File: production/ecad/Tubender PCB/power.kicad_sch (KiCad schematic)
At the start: 68 parts, among them J30 640387-2, U1 LMR36520FADDAR, U12 LM5146RGYR, U13 LM5017SDX/NOPB, U5 TPSM265R1V5SILR

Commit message: start power layout
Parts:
- CBOOT33, C_BST2, C_BST3, C_C1, C_C2, C_C3, C_HF33, C_ILIM1, C_IN2, C_IN33, C_IN5, C_OUT12, C_OUT2, C_OUT3, C_OUT33, C_SS1, C_VCC2, C_VCC3, C_VCC33, C_VIN1, C_VIN2: footprint (none) -> Capacitor_SMD:C_0805_2012Metric
- D10, D6, D7, D8, D9: footprint WL-SMCW_0603:WL-SMCW_0603 -> ${KIPRJMOD}:WL-SMCW_0603
- J30: footprint 640387-2:TE_640387-2 -> ${KIPRJMOD}:TE_640387-2
- L1, L2, L_SW2: footprint (none) -> Inductor_SMD:L_0805_2012Metric
- R1, R2, R20, R22, R3, R46, R47, R_C1, R_C2, R_FB1, R_FB2, R_ILIM1, R_IND12, R_IND24, R_IND3, R_IND48, R_IND5, R_ON1, R_OUT2, R_PG1, R_RT1, R_UV1, R_UV2, R_UV3, R_UV4, R_VCC1, R_VIN12: footprint (none) -> Resistor_SMD:R_0805_2012Metric
- TP1, TP2, TP3, TP4, TP5: footprint 5006:KEYSTONE_5006 -> ${KIPRJMOD}:KEYSTONE_5006
- U1: footprint LMR36520FADDAR:IC_LMR36520FADDAR -> ${KIPRJMOD}:IC_LMR36520FADDAR
- U12: footprint RGY0020B-MFG -> ${KIPRJMOD}:RGY0020B-MFG
- U13: footprint SDC08B -> ${KIPRJMOD}:SDC08B
- U5: footprint SIL0010C -> ${KIPRJMOD}:SIL0010C
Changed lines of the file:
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@@
 			)
 		)
-		(property "Footprint" "WL-SMCW_0603:WL-SMCW_0603"
+		(property "Footprint" "${KIPRJMOD}:WL-SMCW_0603"
 			(at 210.82 156.21 0)
 			(effects
@@
 			)
 		)
-		(property "Footprint" ""
+		(property "Footprint" "Capacitor_SMD:C_0805_2012Metric"
 			(at 94.9452 78.74 0)
 			(effects
@@
 			)
 		)
-		(property "Footprint" "5006:KEYSTONE_5006"
+		(property "Footprint" "${KIPRJMOD}:KEYSTONE_5006"
 			(at 187.96 142.24 0)
 			(effects
@@
 			)
 		)
-		(property "Footprint" "RGY0020B-MFG"
+		(property "Footprint" "${KIPRJMOD}:RGY0020B-MFG"
 			(at 49.53 118.11 0)
 			(effects
@@
 			)
 		)
-		(property "Footprint" "SDC08B"
+		(property "Footprint" "${KIPRJMOD}:SDC08B"
 			(at 35.56 59.69 0)
 			(effects
@@
 			)
 		)
-		(property "Footprint" ""
+		(property "Footprint" "Capacitor_SMD:C_0805_2012Metric"
 			(at 144.78 142.24 0)
 			(effects
@@
 			)
 		)
-		(property "Footprint" ""
+		(property "Footprint" "Resistor_SMD:R_0805_2012Metric"
 			(at 40.64 138.43 0)
 			(effects
@@
 			)
 		)
-		(property "Footprint" ""
+		(property "Footprint" "Resistor_SMD:R_0805_2012Metric"
 			(at 124.46 170.18 0)
 			(effects
@@
 			)
 		)
-		(property "Footprint" ""
+		(property "Footprint" "Resistor_SMD:R_0805_2012Metric"
 			(at 156.21 140.97 0)
 			(effects
@@
 			)
 		)
-		(property "Footprint" ""
+		(property "Footprint" "Capacitor_SMD:C_0805_2012Metric"
 			(at 203.2 96.52 0)
 			(effects
@@
 			)
 		)
-		(property "Footprint" "WL-SMCW_0603:WL-SMCW_0603"
+		(property "Footprint" "${KIPRJMOD}:WL-SMCW_0603"
 			(at 267.97 156.21 0)
 			(effects
@@
 			)
 		)
-		(property "Footprint" ""
+		(property "Footprint" "Capacitor_SMD:C_0805_2012Metric"
 			(at 102.87 139.7 0)
 			(effects
@@
 			)
 		)
-		(property "Footprint" ""
+		(property "Footprint" "Resistor_SMD:R_0805_2012Metric"
 			(at 267.97 147.32 0)
 			(effects
@@
 			)
 		)
-		(property "Footprint" ""
+		(property "Footprint" "Capacitor_SMD:C_0805_2012Metric"
 			(at 104.14 158.75 0)
 			(effects
@@
 			)
 		)
-		(property "Footprint" ""
+		(property "Footprint" "Resistor_SMD:R_0805_2012Metric"
 			(at 144.78 134.62 0)
 			(effects
@@
 			)
 		)
-		(property "Footprint" ""
+		(property "Footprint" "Capacitor_SMD:C_0805_2012Metric"
 			(at 124.1552 72.39 0)
 			(effects
@@
 			)
 		)
-		(property "Footprint" ""
+		(property "Footprint" "Resistor_SMD:R_0805_2012Metric"
 			(at 27.94 123.19 0)
 			(effects
@@
 			)
 		)
-		(property "Footprint" ""
+		(property "Footprint" "Resistor_SMD:R_0805_2012Metric"
 			(at 210.82 147.32 0)
 			(effects
@@
 			)
 		)
-		(property "Footprint" "WL-SMCW_0603:WL-SMCW_0603"
+		(property "Footprint" "${KIPRJMOD}:WL-SMCW_0603"
 			(at 248.92 156.21 0)
 			(effects
@@
 			)
 		)
-		(property "Footprint" "5006:KEYSTONE_5006"
+		(property "Footprint" "${KIPRJMOD}:KEYSTONE_5006"
 			(at 243.84 142.24 0)
 			(effects
@@
 			)
 		)
-		(property "Footprint" ""
+		(property "Footprint" "Capacitor_SMD:C_0805_2012Metric"
 			(at 266.7 85.3948 0)
 			(effects
@@
 			)
 		)
-		(property "Footprint" ""
+		(property "Footprint" "Resistor_SMD:R_0805_2012Metric"
 			(at 41.91 168.91 0)
 			(effects
@@
 			)
 		)
-		(property "Footprint" ""
+		(property "Footprint" "Capacitor_SMD:C_0805_2012Metric"
 			(at 22.86 154.94 0)
 			(effects
@@
 			)
 		)
-		(property "Footprint" ""
+		(property "Footprint" "Capacitor_SMD:C_0805_2012Metric"
 			(at 163.83 162.56 0)
 			(effects
@@
 			)
 		)
-		(property "Footprint" ""
+		(property "Footprint" "Resistor_SMD:R_0805_2012Metric"
 			(at 248.92 147.32 0)
 			(effects
@@
 			)
 		)
-		(property "Footprint" ""
+		(property "Footprint" "Capacitor_SMD:C_0805_2012Metric"
 			(at 34.29 177.8 0)
 			(effects
@@
 			)
 		)
-		(property "Footprint" ""
+		(property "Footprint" "Resistor_SMD:R_0805_2012Metric"
 			(at 250.444 50.546 90)
 			(effects
@@
 			)
 		)
-		(property "Footprint" ""
+		(property "Footprint" "Resistor_SMD:R_0805_2012Metric"
 			(at 114.3 158.75 0)
 			(effects
@@
 			)
 		)
-		(property "Footprint" ""
+		(property "Footprint" "Resistor_SMD:R_0805_2012Metric"
 			(at 258.064 97.536 90)
 			(effects
@@
 			)
 		)
-		(property "Footprint" "LMR36520FADDAR:IC_LMR36520FADDAR"
+		(property "Footprint" "${KIPRJMOD}:IC_LMR36520FADDAR"
 			(at 243.84 99.06 0)
 			(effects
@@
 			)
 		)
-		(property "Footprint" ""
+		(property "Footprint" "Capacitor_SMD:C_0805_2012Metric"
 			(at 187.96 41.91 0)
 			(effects
@@
 			)
 		)
-		(property "Footprint" "5006:KEYSTONE_5006"
+		(property "Footprint" "${KIPRJMOD}:KEYSTONE_5006"
 			(at 205.74 142.24 0)
 			(effects
@@
 			)
 		)
-		(property "Footprint" ""
+		(property "Footprint" "Capacitor_SMD:C_0805_2012Metric"
 			(at 193.04 96.52 0)
 			(effects
@@
 			)
 		)
-		(property "Footprint" "SIL0010C"
+		(property "Footprint" "${KIPRJMOD}:SIL0010C"
 			(at 223.52 45.72 0)
 			(effects
@@
 			)
 		)
-		(property "Footprint" ""
+		(property "Footprint" "Resistor_SMD:R_0805_2012Metric"
 			(at 113.284 67.056 90)
 			(effects
@@
 			)
 		)
-		(property "Footprint" ""
+		(property "Footprint" "Inductor_SMD:L_0805_2012Metric"
 			(at 107.95 63.5 0)
 			(effects
@@
 			)
 		)
-		(property "Footprint" ""
+		(property "Footprint" "Resistor_SMD:R_0805_2012Metric"
 			(at 250.444 40.386 90)
 			(effects
@@
 			)
 		)
-		(property "Footprint" ""
+		(property "Footprint" "Capacitor_SMD:C_0805_2012Metric"
 			(at 100.33 125.73 0)
 			(effects
@@
 			)
 		)
-		(property "Footprint" ""
+		(property "Footprint" "Capacitor_SMD:C_0805_2012Metric"
 			(at 30.1752 64.77 0)
 			(effects
@@
 			)
 		)
-		(property "Footprint" ""
+		(property "Footprint" "Resistor_SMD:R_0805_2012Metric"
 			(at 229.87 147.32 0)
 			(effects
@@
 			)
 		)
-		(property "Footprint" "5006:KEYSTONE_5006"
+		(property "Footprint" "${KIPRJMOD}:KEYSTONE_5006"
 			(at 262.89 142.24 0)
 			(effects
@@
 			)
 		)
-		(property "Footprint" "640387-2:TE_640387-2"
+		(property "Footprint" "${KIPRJMOD}:TE_640387-2"
 			(at 140.97 27.94 0)
 			(effects
@@
 			)
 		)
-		(property "Footprint" ""
+		(property "Footprint" "Resistor_SMD:R_0805_2012Metric"
 			(at 208.28 106.68 0)
 			(effects
@@
 			)
 		)
-		(property "Footprint" ""
+		(property "Footprint" "Resistor_SMD:R_0805_2012Metric"
 			(at 40.64 153.67 0)
 			(effects
@@
 			)
 		)
-		(property "Footprint" ""
+		(property "Footprint" "Capacitor_SMD:C_0805_2012Metric"
 			(at 40.64 146.05 0)
 			(effects
@@
 			)
 		)
-		(property "Footprint" ""
+		(property "Footprint" "Capacitor_SMD:C_0805_2012Metric"
 			(at 261.62 41.91 0)
 			(effects
@@
 			)
 		)
-		(property "Footprint" "WL-SMCW_0603:WL-SMCW_0603"
+		(property "Footprint" "${KIPRJMOD}:WL-SMCW_0603"
 			(at 193.04 156.21 0)
 			(effects
@@
 			)
 		)
-		(property "Footprint" ""
+		(property "Footprint" "Resistor_SMD:R_0805_2012Metric"
 			(at 113.284 75.946 90)
 			(effects
@@
 			)
 		)
-		(property "Footprint" ""
+		(property "Footprint" "Resistor_SMD:R_0805_2012Metric"
 			(at 109.22 137.16 0)
 			(effects
@@
 			)
 		)
-		(property "Footprint" ""
+		(property "Footprint" "Capacitor_SMD:C_0805_2012Metric"
 			(at 97.4852 59.69 0)
 			(effects
@@
 			)
 		)
-		(property "Footprint" ""
+		(property "Footprint" "Resistor_SMD:R_0805_2012Metric"
 			(at 201.93 106.68 0)
 			(effects
@@
 			)
 		)
-		(property "Footprint" ""
+		(property "Footprint" "Resistor_SMD:R_0805_2012Metric"
 			(at 193.04 147.32 0)
 			(effects
@@
 			)
 		)
-		(property "Footprint" ""
+		(property "Footprint" "Resistor_SMD:R_0805_2012Metric"
 			(at 49.784 59.436 90)
 			(effects
@@
 			)
 		)
-		(property "Footprint" "WL-SMCW_0603:WL-SMCW_0603"
+		(property "Footprint" "${KIPRJMOD}:WL-SMCW_0603"
 			(at 229.87 156.21 0)
 			(effects
@@
 			)
 		)
-		(property "Footprint" ""
+		(property "Footprint" "Resistor_SMD:R_0805_2012Metric"
 			(at 42.164 75.946 90)
 			(effects
@@
 			)
 		)
-		(property "Footprint" ""
+		(property "Footprint" "Inductor_SMD:L_0805_2012Metric"
 			(at 217.17 106.68 0)
 			(effects
@@
 			)
 		)
-		(property "Footprint" ""
+		(property "Footprint" "Resistor_SMD:R_0805_2012Metric"
 			(at 122.174 75.946 90)
 			(effects
@@
 			)
 		)
-		(property "Footprint" ""
+		(property "Footprint" "Capacitor_SMD:C_0805_2012Metric"
 			(at 226.06 104.14 0)
 			(effects
@@
 			)
 		)
-		(property "Footprint" ""
+		(property "Footprint" "Capacitor_SMD:C_0805_2012Metric"
 			(at 207.01 113.03 0)
 			(effects
@@
 			)
 		)
-		(property "Footprint" ""
+		(property "Footprint" "Resistor_SMD:R_0805_2012Metric"
 			(at 27.94 133.35 0)
 			(effects
@@
 			)
 		)
-		(property "Footprint" ""
+		(property "Footprint" "Resistor_SMD:R_0805_2012Metric"
 			(at 42.164 67.056 90)
 			(effects
@@
 			)
 		)
-		(property "Footprint" "5006:KEYSTONE_5006"
+		(property "Footprint" "${KIPRJMOD}:KEYSTONE_5006"
 			(at 224.79 142.24 0)
 			(effects
@@
 			)
 		)
-		(property "Footprint" ""
+		(property "Footprint" "Inductor_SMD:L_0805_2012Metric"
 			(at 133.35 130.81 0)
 			(effects
@@
 			)
 		)
-		(property "Footprint" ""
+		(property "Footprint" "Capacitor_SMD:C_0805_2012Metric"
 			(at 41.91 120.65 0)
 			(effects
@@
 			)
 		)
-		(property "Footprint" ""
+		(property "Footprint" "Capacitor_SMD:C_0805_2012Metric"
 			(at 104.14 166.37 0)
 			(effects
@@
 			)
 		)
-		(property "Footprint" ""
+		(property "Footprint" "Resistor_SMD:R_0805_2012Metric"
 			(at 27.94 113.03 0)
 			(effects

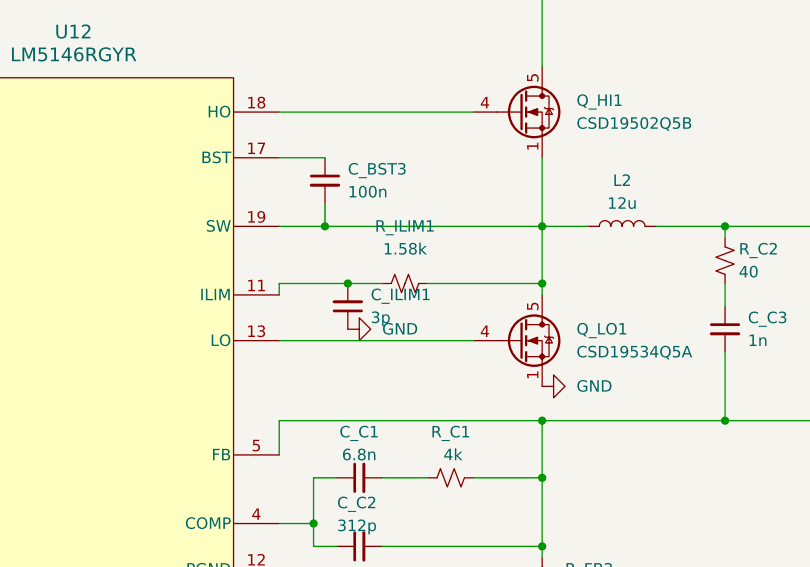
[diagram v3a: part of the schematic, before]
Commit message: layed out most buck architectures, one status led
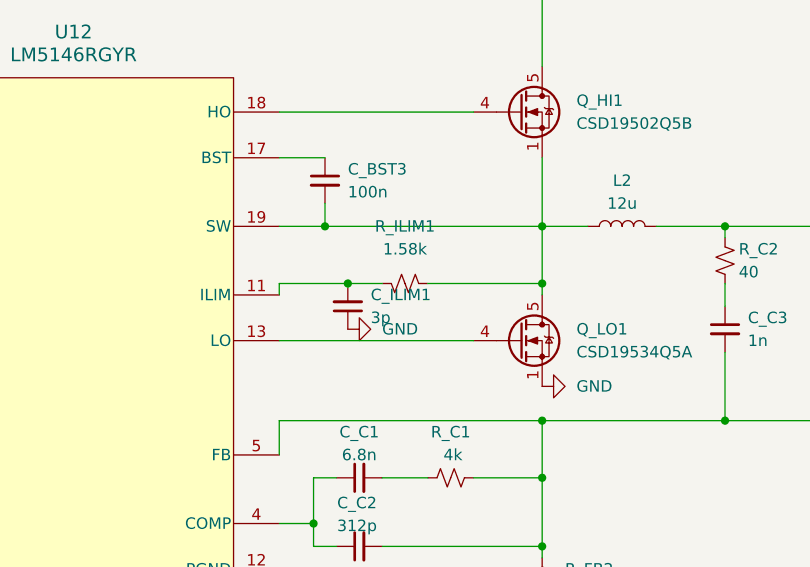
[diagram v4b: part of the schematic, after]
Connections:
- net at C_BST3.2, L2.1, Q_HI1.1 (S)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: now also R_ILIM1.1; no longer R_ILIM1.2
- net at C_ILIM1.2, U12.11 (ILIM): now also R_ILIM1.2; no longer R_ILIM1.1
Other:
- moved on the sheet: R_ILIM1
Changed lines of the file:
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@@
 	(symbol
 		(lib_id "Device:R_Small_US")
-		(at 109.22 137.16 90)
+		(at 109.22 137.16 270)
+		(mirror x)
 		(unit 1)
 		(exclude_from_sim no)
@@
 		(on_board yes)
 		(dnp no)
-		(fields_autoplaced yes)
 		(property "Reference" "R_ILIM1"
 			(at 109.22 130.81 90)

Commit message: Added Testpoints to UI sheet
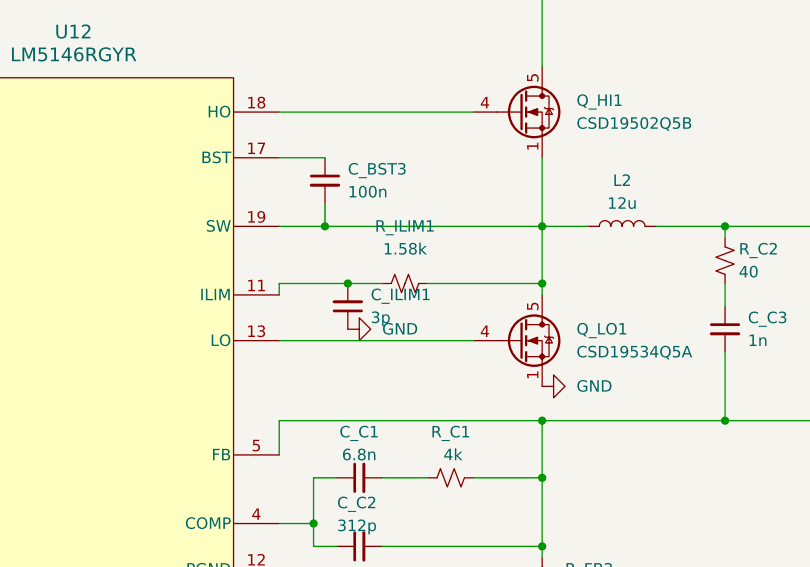
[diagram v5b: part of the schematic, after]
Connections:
- net at C_BST3.2, L2.1, Q_HI1.1 (S)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: now also R_ILIM1.2; no longer R_ILIM1.1
- net at C_ILIM1.2, U12.11 (ILIM): now also R_ILIM1.1; no longer R_ILIM1.2
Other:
- moved on the sheet: R_ILIM1
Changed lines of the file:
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@@
 	(symbol
 		(lib_id "Device:R_Small_US")
-		(at 109.22 137.16 270)
-		(mirror x)
+		(at 109.22 137.16 90)
 		(unit 1)
 		(exclude_from_sim no)
@@
 		(on_board yes)
 		(dnp no)
+		(fields_autoplaced yes)
 		(property "Reference" "R_ILIM1"
 			(at 109.22 130.81 90)

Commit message: got rid of all drc issues
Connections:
- net GND: now also U12.15 (EP), U12.21 (EP)
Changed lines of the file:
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@@
+	)
+	(junction
+		(at 95.25 187.96)
+		(diameter 0)
+		(color 0 0 0 0)
 	)
 	(junction
@@
 	(junction
 		(at 163.83 130.81)
+		(diameter 0)
+		(color 0 0 0 0)
+	)
+	(junction
+		(at 95.25 181.61)
 		(diameter 0)
 		(color 0 0 0 0)
@@
 	(wire
 		(pts
+			(xy 95.25 187.96) (xy 109.22 187.96)
+		)
+		(stroke
+			(width 0)
+			(type default)
+		)
+	)
+	(wire
+		(pts
 			(xy 251.46 36.83) (xy 251.46 35.56)
 		)
@@
 	(wire
 		(pts
+			(xy 95.25 179.07) (xy 95.25 181.61)
+		)
+		(stroke
+			(width 0)
+			(type default)
+		)
+	)
+	(wire
+		(pts
 			(xy 43.18 55.88) (xy 50.8 55.88)
 		)
@@
 	(wire
 		(pts
+			(xy 95.25 181.61) (xy 95.25 187.96)
+		)
+		(stroke
+			(width 0)
+			(type default)
+		)
+	)
+	(wire
+		(pts
 			(xy 114.3 63.5) (xy 111.76 63.5)
 		)
@@
 	(wire
 		(pts
-			(xy 34.29 187.96) (xy 109.22 187.96)
-		)
-		(stroke
+			(xy 34.29 187.96) (xy 95.25 187.96)
+		)
+		(stroke

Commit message: ok
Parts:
- CBOOT33: value 0.1u -> 0.1uF
- C_BST3, C_VIN1: value 100n -> 100nF
- C_C1: value 6.8n -> 6.8nF
- C_C2: value 312p -> 312pF
- C_C3: value 1n -> 1nF
- C_HF33: value 220n -> 220nF
- C_ILIM1: value 3p -> 3pF
- C_IN2, C_IN33: value 4.7u -> 4.7uF
- C_OUT3: value 10u -> 10uF
- C_OUT33: value 100u -> 100uF
- C_SS1: value 12.5n -> 12.5nF
- C_VCC2: value 2.2u -> 2.2uF
- C_VCC33: value 1u -> 1uF
- L1: value 8.5u -> 8.5uH
- L2: value 12u -> 12uH
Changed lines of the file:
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@@
 			)
 		)
-		(property "Value" "1n"
+		(property "Value" "1nF"
 			(at 147.32 143.5162 0)
 			(effects
@@
 			)
 		)
-		(property "Value" "220n"
+		(property "Value" "220nF"
 			(at 205.232 96.774 0)
 			(effects
@@
 			)
 		)
-		(property "Value" "3p"
+		(property "Value" "3pF"
 			(at 105.41 140.9635 0)
 			(effects
@@
 			)
 		)
-		(property "Value" "6.8n"
+		(property "Value" "6.8nF"
 			(at 104.14 156.21 90)
 			(effects
@@
 			)
 		)
-		(property "Value" "1u"
+		(property "Value" "1uF"
 			(at 262.89 81.28 90)
 			(effects
@@
 			)
 		)
-		(property "Value" "4.7u"
+		(property "Value" "4.7uF"
 			(at 16.002 155.956 0)
 			(effects
@@
 			)
 		)
-		(property "Value" "2.2u"
+		(property "Value" "2.2uF"
 			(at 36.83 179.0762 0)
 			(effects
@@
 			)
 		)
-		(property "Value" "4.7u"
+		(property "Value" "4.7uF"
 			(at 187.198 97.79 0)
 			(effects
@@
 			)
 		)
-		(property "Value" "100n"
+		(property "Value" "100nF"
 			(at 102.87 127.0062 0)
 			(effects
@@
 			)
 		)
-		(property "Value" "12.5n"
+		(property "Value" "12.5nF"
 			(at 40.64 143.51 90)
 			(effects
@@
 			)
 		)
-		(property "Value" "10u"
+		(property "Value" "10uF"
 			(at 264.16 43.1862 0)
 			(effects
@@
 			)
 		)
-		(property "Value" "8.5u"
+		(property "Value" "8.5uH"
 			(at 217.17 104.14 90)
 			(effects
@@
 			)
 		)
-		(property "Value" "0.1u"
+		(property "Value" "0.1uF"
 			(at 226.06 109.982 90)
 			(effects
@@
 			)
 		)
-		(property "Value" "100u"
+		(property "Value" "100uF"
 			(at 205.994 118.11 90)
 			(effects
@@
 			)
 		)
-		(property "Value" "12u"
+		(property "Value" "12uH"
 			(at 133.35 128.27 90)
 			(effects
@@
 			)
 		)
-		(property "Value" "100n"
+		(property "Value" "100nF"
 			(at 44.45 121.9262 0)
 			(effects
@@
 			)
 		)
-		(property "Value" "312p"
+		(property "Value" "312pF"
 			(at 103.886 164.084 90)
 			(effects

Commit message: lfg!!!
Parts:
- C_OUT12: value 22u -> 22uF
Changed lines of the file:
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@@
 			)
 		)
-		(property "Value" "22u"
+		(property "Value" "22uF"
 			(at 166.37 163.8362 0)
 			(effects
